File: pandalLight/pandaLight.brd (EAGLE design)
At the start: 90 x 57.4 mm, 113 parts, among them J1 PJ-037A, U1 MIC2230-XXYML, U10 LEDS_CON, U11 LEDS_CON, U12 TPD12S016PWR, U13 M25P40-VMN, U14 PMOD-2X6, U15 PMOD-2X6, U16 PLR135-T10, U17 PLT133-T10W, U18 TP10SQ, U19 TP10SQ, U2 6SLX9TQG144, U20 PAN1322, U3 93LC46BT-I/OT, U4 FT2232HL, U5 TPD12S016PWR, U6 51, U7 51, U8 TXB0104RGYR, U9 100k, X1 USBUB-S, X2 HDMI_RECEPTICAL_A, X3 HDMI_RECEPTICAL_A, Y1 403, Y2 20Mhz

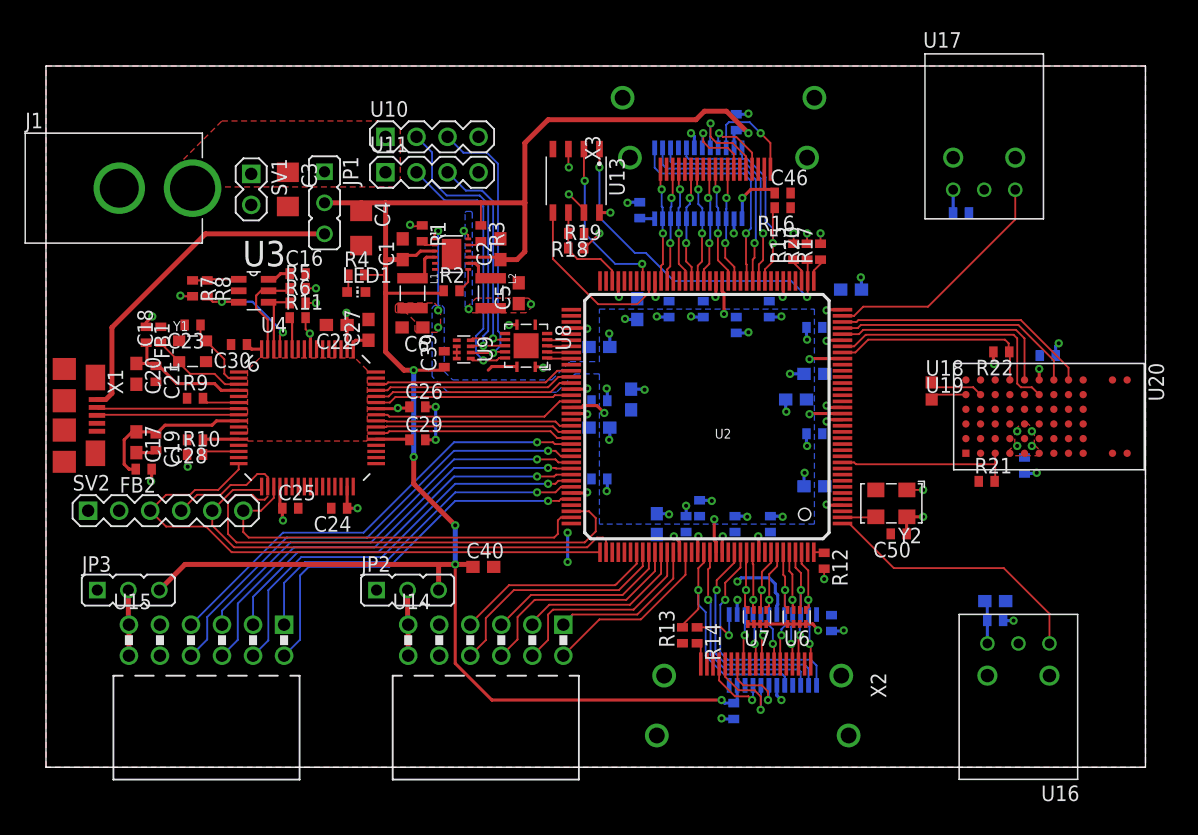
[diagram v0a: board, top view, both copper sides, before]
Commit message: No more airwires! Added ESD protection at 5V_SUP
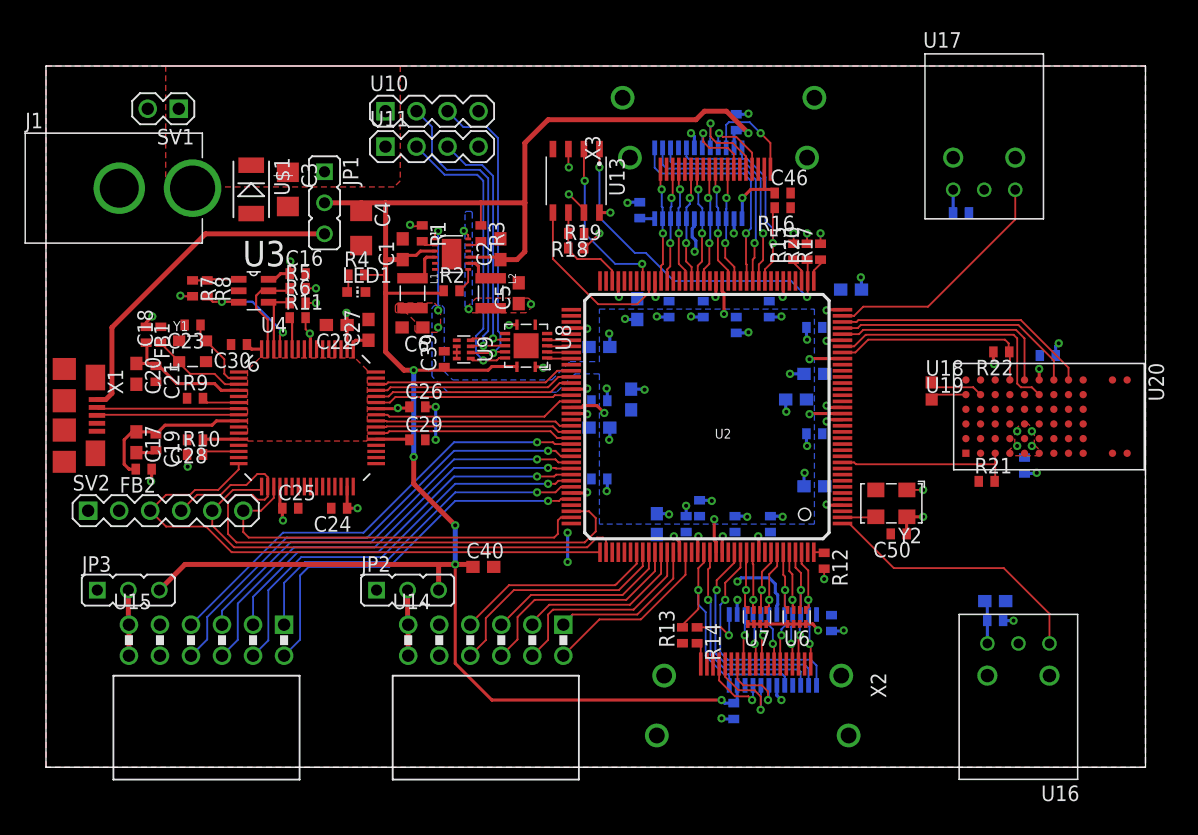
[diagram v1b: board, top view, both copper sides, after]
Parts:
- added U$1: 6V, pandaLight:DO-214AC
- moved SV1 9.77 mm to (9.60, 53.9), turned to 180 degrees
- moved U10 2.10 mm to (31.6, 53.7)
- moved U11 2.10 mm to (31.6, 50.8)
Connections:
- net 5V_SUP: now also U$1.C
- net GND: now also U$1.A
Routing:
- net +5V: track 166.4 -> 170.3 mm
- net LEDS1_DATA_5V: track 24.1 -> 26.2 mm
- net LEDS1_CLK_5V: track 23.7 -> 25.8 mm
- net LEDS0_CLK_5V: track 18.8 -> 20.9 mm
- net LEDS0_DATA_5V: track 22.7 -> 24.8 mm
- net GND: track 51.2 -> 53.3 mm, vias 37 -> 38
- net +3V3: track 70.7 -> 71.9 mm, vias 51 -> 52
- net HDMI_RX_CTRL_EN: track 20.4 -> 21.3 mm
- net USB_TDO: track 49.7 -> 50.5 mm

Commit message: Move S6LX9 to own library; Adjusted parts' "place" layer; USB_PWRSAV#
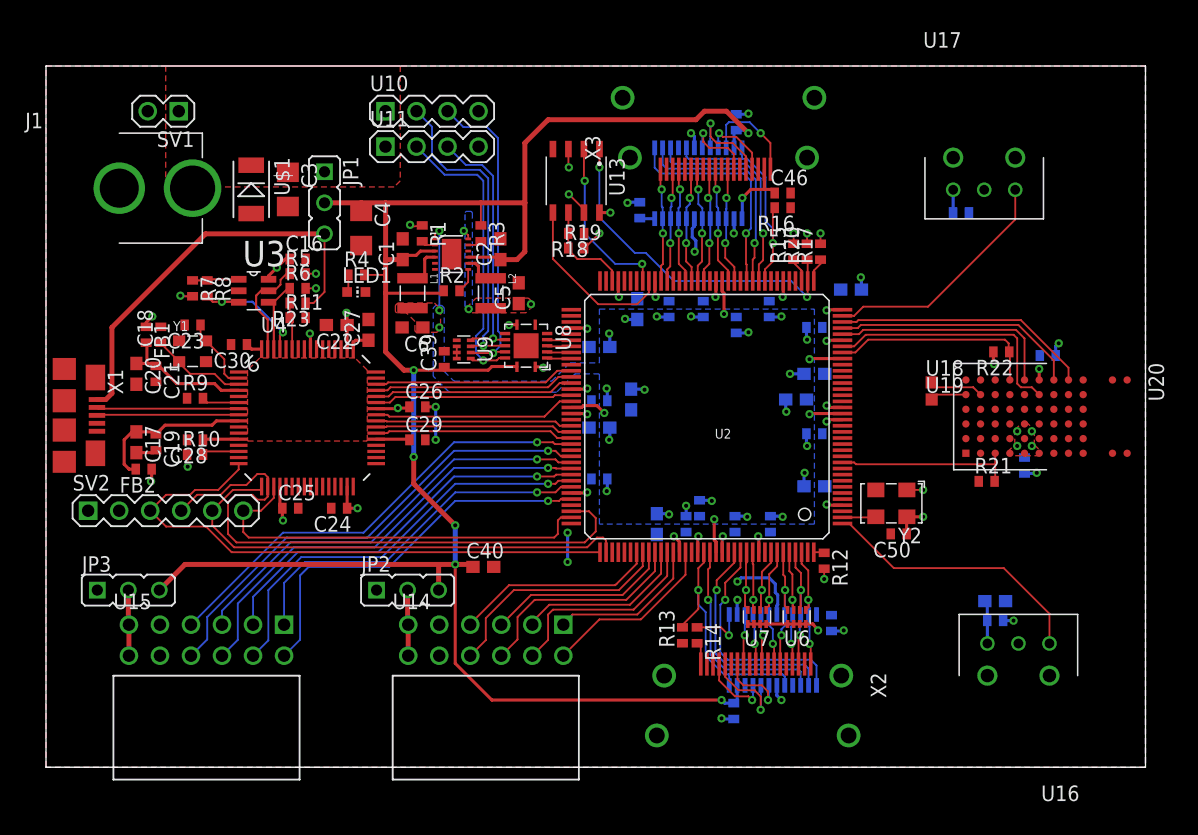
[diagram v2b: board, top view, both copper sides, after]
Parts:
- added R23: 4.7k, pandaLight:0402
- U2: device xilinx_devices_V6:TQ144 -> pandaLight:TQ144
- moved C16 1.20 mm to (20.6, 41.6)
- moved R6 1.20 mm to (20.6, 39.2)
- moved R5 1.20 mm to (20.6, 40.4)
- moved SV1 0.20 mm to (9.60, 53.7)
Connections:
- removed net USB_SUSPEND#: U4.36
- net +3V3: no longer R11.2
- net GND: now also R11.2
- net USB_PWRSAVE#: now also R23.2
- net USB_VBUS: now also R23.1
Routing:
- net USB_VBUS: track 27.4 -> 34.1 mm
- net +3V3: track 71.9 -> 70.1 mm
- net USB_PWRSAVE#: track 2.66 -> 3.86 mm
- net N$6: track 7.77 -> 8.50 mm

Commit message: Part renumber; "place" layer changes
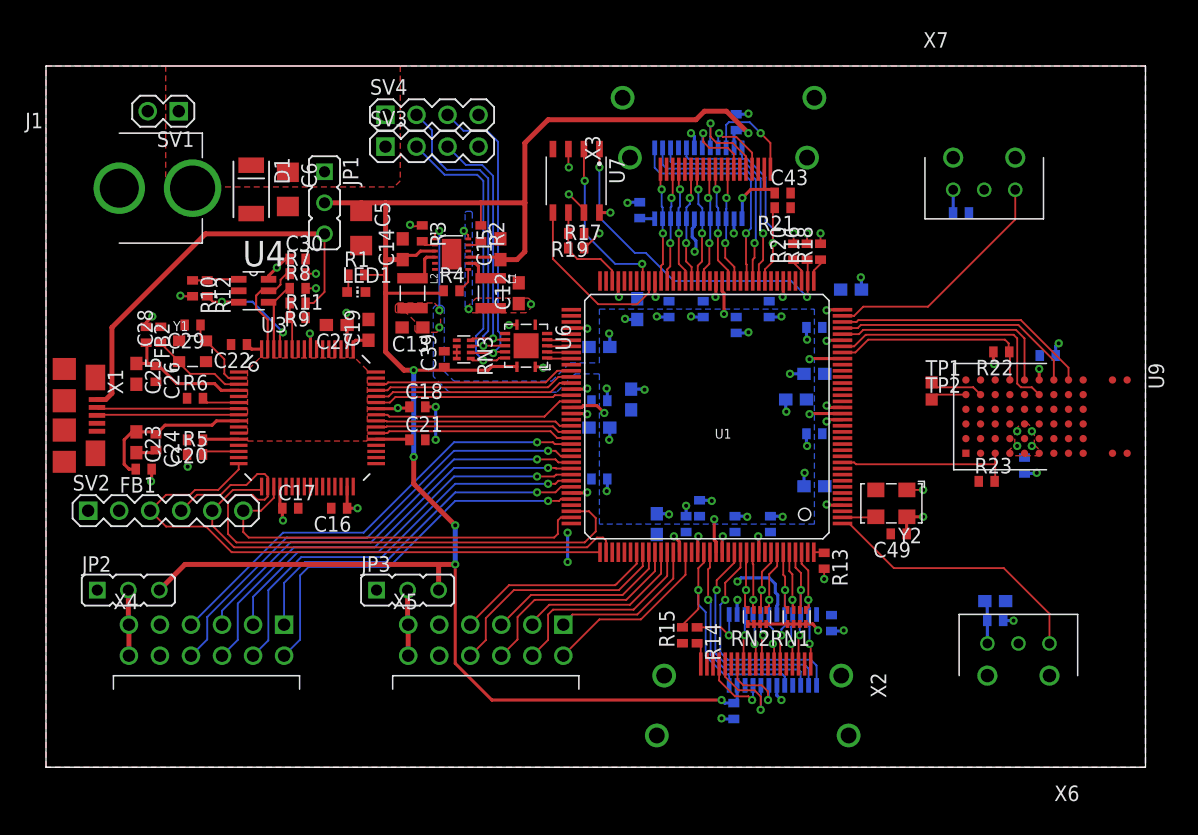
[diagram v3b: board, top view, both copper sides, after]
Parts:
- removed C54: 0.1u, pandaLight:0402
- removed U10: LEDS_CON, pandaLight:MA04-1
- removed U12: TPD12S016PWR, pandaLight:PW_R-PDSO-G24
- removed U13: M25P40-VMN, pandaLight:SO8N
- removed U20: PAN1322, pandaLight:PAN1322
- added RN1, RN2: 51, pandaLight:741C083
- added RN3: 100k, pandaLight:741C083
- added SV4: LEDS_CON, pandaLight:MA04-1
- C10, C11, C41, C47: value 4.7u -> 0.47u; device pandaLight:0603 -> pandaLight:0402
- C12, C13: value 0.47u -> 10u; device pandaLight:0402 -> pandaLight:0603
- C14, C15: value 0.47u -> 4.7u; device pandaLight:0402 -> pandaLight:0603
- C17, C20, C22: value 4.7u -> 0.1u; device pandaLight:0603 -> pandaLight:0402
- C18: value 27p -> 0.1u
- C19, C25, C46: value 0.1u -> 4.7u; device pandaLight:0402 -> pandaLight:0603
- C23: value 27p -> 4.7u; device pandaLight:0402 -> pandaLight:0603
- C28, C29: value 0.1u -> 27p
- C3, C4: value 100u -> 0.47u; device pandaLight:1206 -> pandaLight:0402
- C43, C49: value 0.47u -> 0.1u
- C5, C6: value 10u -> 100u; device pandaLight:0603 -> pandaLight:1206
- JP2: value PMOD2-3_VCC_SEL -> PMOD0-1_VCC_SEL
- JP3: value PMOD0-1_VCC_SEL -> PMOD2-3_VCC_SEL
- R1: value 100k -> 1k
- R12: value 1k -> 2.2k
- R13: value 10k -> 1k
- R15, R21: value 4.7k -> 10k
- R16: value 10k -> 2.4k
- R17: value 4.7k -> 100
- R18: value 100 -> 4.7k
- R20: value 2.4k -> 4.7k
- R4: value 1k -> 100k
- R6: value 10k -> 12k
- R8: value 2.2k -> 10k
- R9: value 12k -> 4.7k
- U1: value MIC2230-XXYML -> 6SLX9TQG144; device pandaLight:MLF-12 -> pandaLight:TQ144
- U2: value 6SLX9TQG144 -> MIC2230-XXYML; device pandaLight:TQ144 -> pandaLight:MLF-12
- U3: value 93LC46BT-I/OT -> FT2232HL; device pandaLight:SOT23-6 -> pandaLight:LQFP64
- U4: value FT2232HL -> 93LC46BT-I/OT; device pandaLight:LQFP64 -> pandaLight:SOT23-6
- U6: value 51 -> TXB0104RGYR; device pandaLight:741C083 -> pandaLight:S-PVQFN-N14
- U7: value 51 -> M25P40-VMN; device pandaLight:741C083 -> pandaLight:SO8N
- U8: value TXB0104RGYR -> TPD12S016PWR; device pandaLight:S-PVQFN-N14 -> pandaLight:PW_R-PDSO-G24
- U9: value 100k -> PAN1322; device pandaLight:741C083 -> pandaLight:PAN1322
- moved R23 58.3 mm to (77.0, 23.4), turned to 0 degrees
- moved R12 55.2 mm to (13.2, 39.2)
- moved U9 48.0 mm to (81.9, 28.7)
- moved U7 38.6 mm to (43.4, 48.0), turned to 270 degrees
- moved C3 38.3 mm to (56.5, 36.2), flipped to the bottom
- moved C4 35.9 mm to (53.5, 21.2), flipped to the bottom, turned to 90 degrees
- moved C51 33.5 mm to (74.9, 45.4), turned to 0 degrees
- moved R15 32.7 mm to (52.1, 10.8)
- moved C14 32.2 mm to (29.2, 42.4), flipped to the top
- moved U6 31.4 mm to (39.3, 34.5), turned to 270 degrees
- moved C15 29.6 mm to (37.2, 42.4), flipped to the top
- moved R21 27.9 mm to (60.3, 45.8), turned to 180 degrees
- moved C2 27.1 mm to (61.4, 30.1), flipped to the bottom, turned to 0 degrees
- moved U1 24.8 mm to (54.1, 28.7), turned to 180 degrees
- moved U2 24.8 mm to (33.2, 42.0), turned to 0 degrees
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- renumbered U$1 to D1, U11 to SV3, U14 to X5, U15 to X4, U16 to X6, U17 to X7, U18 to TP1, U19 to TP2
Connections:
- net +1V2: now also C1.1, C13.1, C2.1, C3.1, C4.1, L2.2, U1.P128, U1.P19, U1.P28, U1.P52, U1.P89, U2.1; no longer C10.1, C12.1, C14.1, C6.1, C8.1, L1.2, U1.1, U2.P128, U2.P19, U2.P28, U2.P52, U2.P89
- net +1V8: now also C19.1, C20.1, C21.1, C22.1, U3.12, U3.37, U3.49, U3.64; no longer C27.1, C28.1, C29.1, C30.1, U4.12, U4.37, U4.49, U4.64
- net +3V3: now also C10.1, C12.1, C17.1, C18.1, C27.1, C30.1, C40.1, C46.1, C51.1, C8.1, L1.2, R10.2, R13.2, R16.2, R18.2, R3.1, R5.1, R8.2, RN1.5, RN1.6, RN1.7, RN1.8, RN2.5, RN2.6, RN2.7, RN2.8, U1.P103, U1.P122, U1.P125, U1.P129, U1.P135, U1.P18, U1.P20, U1.P31, U1.P36, U1.P4, U1.P42, U1.P53, U1.P63, U1.P69, U1.P76, U1.P86, U1.P90, U2.12, U3.20, U3.31, U3.42, U3.50, U3.56, U4.6, U6.1, U7.3, U8.24, U9.A4, U9.A5, U9.A6, U9.B5, U9.C5, U9.F6; no longer C13.1, C15.1, C22.1, C24.1, C25.1, C26.1, C43.1, C5.1, C50.1, C54.1, L2.2, R1.1, R10.1, R12.2, R15.2, R19.2, R5.2, R6.2, U1.12, U12.24, U13.3, U13.7, U13.8, U2.P103, U2.P122, U2.P125, U2.P129, U2.P135, U2.P18, U2.P20, U2.P31, U2.P36, U2.P4, U2.P42, U2.P53, U2.P63, U2.P69, U2.P76, U2.P86, U2.P90, U20.A4, U20.A5, U20.A6, U20.B5, U20.C5, U20.F6, U3.6, U4.20, U4.31, U4.42, U4.50, U4.56, U6.5, U6.6, U6.7, U7.5, U7.6, U8.1, U8.8
- net +5V: now also C14.1, C15.1, C5.1, R1.2, R4.1, U2.3, U2.9, U6.14, U8.11; no longer C1.1, C2.1, C4.1, C40.1, R3.1, R4.2, U1.3, U1.9, U12.11, U8.14
- net 5V_SUP: now also C6.1, SV4.1; no longer C3.1, U10.1
- net BT_CTS: now also U1.P32, U9.F5; no longer U2.P32, U20.F5
- net BT_RESET#: now also R23.2, U1.P11, U9.A3; no longer R21.2, U2.P11, U20.A3
- net BT_RTS: now also U1.P34, U9.F8; no longer U2.P34, U20.F8
- net BT_RX: now also U1.P30, U9.E6; no longer U2.P30, U20.E6
- net BT_TX: now also U1.P33, U9.F7; no longer U2.P33, U20.F7
- net BT_WAKE: now also U1.P29, U9.F4; no longer U2.P29, U20.F4
- net FPGA_CLK20: now also U1.P2; no longer U2.P2
- net GND: now also R15.1, R19.1, R23.1, R6.1, RN3.1, RN3.2, RN3.3, RN3.4, SV4.4, U1.P108, U1.P113, U1.P13, U1.P130, U1.P136, U1.P25, U1.P3, U1.P49, U1.P54, U1.P60, U1.P68, U1.P73, U1.P77, U1.P91, U1.P96, U2.5, U2.6, U2.EP, U3.1, U3.10, U3.11, U3.13, U3.15, U3.25, U3.35, U3.47, U3.5, U3.51, U4.2, U6.7, U6.EP, U7.4, U8.14, U8.19, U8.6, U9.A1, U9.A11, U9.A12, U9.A7, U9.A9, U9.C8, U9.C9, U9.D7, U9.D8, U9.E8, U9.E9, U9.F1, U9.F11, U9.F12, U9.F9; no longer C54.2, R13.1, R16.1, R18.1, R9.1, U1.5, U1.6, U1.EP, U10.4, U12.14, U12.19, U12.6, U13.4, U2.P108, U2.P113, U2.P13, U2.P130, U2.P136, U2.P25, U2.P3, U2.P49, U2.P54, U2.P60, U2.P68, U2.P73, U2.P77, U2.P91, U2.P96, U20.A1, U20.A11, U20.A12, U20.A7, U20.A9, U20.C8, U20.C9, U20.D7, U20.D8, U20.E8, U20.E9, U20.F1, U20.F11, U20.F12, U20.F9, U3.2, U4.1, U4.10, U4.11, U4.13, U4.15, U4.25, U4.35, U4.47, U4.5, U4.51, U8.7, U8.EP, U9.1, U9.2, U9.3, U9.4
- net HDMI_RX_CEC_3V3: now also U1.P132; no longer U2.P132
- net HDMI_RX_CLK_N: now also RN2.4, U1.P133; no longer U2.P133, U7.4
- net HDMI_RX_CLK_P: now also RN2.3, U1.P134; no longer U2.P134, U7.3
- net HDMI_RX_CTRL_EN: now also R15.2, U1.P126; no longer R13.2, U2.P126
- net HDMI_RX_DATA0_N: now also RN2.2, U1.P137; no longer U2.P137, U7.2
- net HDMI_RX_DATA0_P: now also RN2.1, U1.P138; no longer U2.P138, U7.1
- net HDMI_RX_DATA1_N: now also RN1.4, U1.P139; no longer U2.P139, U6.4
- net HDMI_RX_DATA1_P: now also RN1.3, U1.P140; no longer U2.P140, U6.3
- net HDMI_RX_DATA2_N: now also RN1.2, U1.P141; no longer U2.P141, U6.2
- net HDMI_RX_DATA2_P: now also RN1.1, U1.P142; no longer U2.P142, U6.1
- net HDMI_RX_SCL_3V3: now also U1.P131; no longer U2.P131
- net HDMI_RX_SDA_3V3: now also U1.P127; no longer U2.P127
- net HDMI_TX_5V: now also C43.1, U8.13; no longer C46.1, U12.13
- net HDMI_TX_CEC: now also U8.7; no longer U12.7
- net HDMI_TX_CEC_3V3: now also U1.P48, U8.1; no longer U12.1, U2.P48
- net HDMI_TX_CLK_N: now also U1.P50, U8.15; no longer U12.15, U2.P50
- net HDMI_TX_CLK_P: now also U1.P51, U8.16; no longer U12.16, U2.P51
- net HDMI_TX_CTRL_EN: now also R21.2, U1.P45, U8.12, U8.5; no longer R16.2, U12.12, U12.5, U2.P45
- net HDMI_TX_DATA0_N: now also U1.P55, U8.17; no longer U12.17, U2.P55
- net HDMI_TX_DATA0_P: now also U1.P56, U8.18; no longer U12.18, U2.P56
- net HDMI_TX_DATA1_N: now also U1.P57, U8.20; no longer U12.20, U2.P57
- net HDMI_TX_DATA1_P: now also U1.P58, U8.21; no longer U12.21, U2.P58
- net HDMI_TX_DATA2_N: now also U1.P61, U8.22; no longer U12.22, U2.P61
- net HDMI_TX_DATA2_P: now also U1.P62, U8.23; no longer U12.23, U2.P62
- net HDMI_TX_HPD_5V: now also U8.10; no longer U12.10
- net HDMI_TX_SCL_3V3: now also U1.P47, U8.2; no longer U12.2, U2.P47
- net HDMI_TX_SCL_5V: now also U8.8; no longer U12.8
- net HDMI_TX_SDA_3V3: now also U1.P46, U8.3; no longer U12.3, U2.P46
- net HDMI_TX_SDA_5V: now also U8.9; no longer U12.9
- net LEDS0_CLK: now also U1.P78, U6.5; no longer U2.P78, U8.5
- net LEDS0_CLK_5V: now also RN3.8, U6.10; no longer U8.10, U9.8
- net LEDS0_DATA: now also U1.P81, U6.2; no longer U2.P81, U8.2
- net LEDS0_DATA_5V: now also RN3.5, U6.13; no longer U8.13, U9.5
- net LEDS1_CLK: now also U1.P80, U6.3; no longer U2.P80, U8.3
- net LEDS1_CLK_5V: now also RN3.6, SV4.3, U6.12; no longer U10.3, U8.12, U9.6
- net LEDS1_DATA: now also U1.P79, U6.4; no longer U2.P79, U8.4
- net LEDS1_DATA_5V: now also RN3.7, SV4.2, U6.11; no longer U10.2, U8.11, U9.7
- net N$1: now also C29.1, U3.2; no longer C23.1, U4.2
- net N$10: now also R12.2, U3.61, U4.3; no longer R8.2, U3.3, U4.61
- net N$11: now also R6.2, U3.6; no longer R9.2, U4.6
- net N$12: now also R10.1, R12.1, U4.1; no longer R7.1, R8.1, U3.1
- net N$13: now also R5.2, U3.14; no longer R10.2, U4.14
- net N$19: now also U9.E1; no longer U20.E1
- net N$25: now also R2.2, U2.11; no longer R3.2, U1.11
- net N$27: now also R3.2, U2.2; no longer R1.2, U1.2
- net N$28: now also C25.1, C26.1, FB2.2, U3.4; no longer C20.1, C21.1, FB1.2, U4.4
- net N$29: now also U9.E2; no longer U20.E2
- net N$31: now also C23.1, C24.1, FB1.2, U3.9; no longer C17.1, C19.1, FB2.2, U4.9
- net N$34: now also R18.1, U1.P37; no longer R17.1, U2.P37
- net N$35: now also R13.1, U1.P144; no longer R12.1, U2.P144
- net N$36: now also C50.1; no longer C51.1
- net N$39: now also R20.1, U1.P39; no longer R15.1, U2.P39
- net N$4: now also R4.2, U2.7; no longer R2.2, U1.7
- net N$40: now also U1.P64, U7.5; no longer U13.5, U2.P64
- net N$41: now also R16.1, U1.P38, U7.1; no longer R20.1, U13.1, U2.P38
- net N$42: now also R17.1, R19.2, U1.P70, U7.6; no longer R18.2, R19.1, U13.6, U2.P70
- net N$43: now also U1.P65, U7.2; no longer U13.2, U2.P65
- net N$47: now also R1.1; no longer R4.1
- net N$49: now also JP3.2; no longer JP2.2
- net N$5: now also C28.1, U3.3; no longer C18.1, U4.3
- net N$51: now also JP2.2; no longer JP3.2
- net N$6: now also R7.1, U3.63, U4.5; no longer R5.1, U3.5, U4.63
- net N$7: now also U3.7; no longer U4.7
- net N$8: now also U3.8; no longer U4.8
- net N$9: now also R8.1, U3.62, U4.4; no longer R6.1, U3.4, U4.62
- net PMOD0_0: now also U1.P102; no longer U2.P102
- net PMOD0_1: now also U1.P100; no longer U2.P100
- net PMOD0_2: now also U1.P98; no longer U2.P98
- net PMOD0_3: now also U1.P95; no longer U2.P95
- net PMOD1_0: now also U1.P104; no longer U2.P104
- net PMOD1_1: now also U1.P101; no longer U2.P101
- net PMOD1_2: now also U1.P99; no longer U2.P99
- net PMOD1_3: now also U1.P97; no longer U2.P97
- net PMOD2_0: now also U1.P121; no longer U2.P121
- net PMOD2_1: now also U1.P119; no longer U2.P119
- net PMOD2_2: now also U1.P117; no longer U2.P117
- net PMOD2_3: now also U1.P115; no longer U2.P115
- net PMOD3_0: now also U1.P123; no longer U2.P123
- net PMOD3_1: now also U1.P120; no longer U2.P120
- net PMOD3_2: now also U1.P118; no longer U2.P118
- net PMOD3_3: now also U1.P116; no longer U2.P116
- net SW1: now also L1.1, U2.8; no longer L2.1, U1.8
- net SW2: now also L2.1, U2.4; no longer L1.1, U1.4
- net TOS_IN: now also U1.P1; no longer U2.P1
- net TOS_OUT: now also U1.P35; no longer U2.P35
- net USB_CTS#: now also U1.P88, U3.41; no longer U2.P88, U4.41
- net USB_DCD#: now also U1.P84, U3.45; no longer U2.P84, U4.45
- net USB_DSR#: now also U1.P85, U3.44; no longer U2.P85, U4.44
- net USB_DTR#: now also U1.P87, U3.43; no longer U2.P87, U4.43
- net USB_PWRSAVE#: now also R9.2, U3.59; no longer R23.2, U4.59
- net USB_RI#: now also U1.P83, U3.46; no longer U2.P83, U4.46
- net USB_RTS#: now also U1.P92, U3.40; no longer U2.P92, U4.40
- net USB_RXD: now also U1.P93, U3.39; no longer U2.P93, U4.39
- net USB_TCK: now also U1.P109, U3.16; no longer U2.P109, U4.16
- net USB_TDI: now also U1.P110, U3.17; no longer U2.P110, U4.17
- net USB_TDO: now also U1.P106, U3.18; no longer U2.P106, U4.18
- net USB_TMS: now also U1.P107, U3.19; no longer U2.P107, U4.19
- net USB_TXD: now also U1.P94, U3.38; no longer U2.P94, U4.38
- net USB_VBUS: now also R9.1; no longer R23.1
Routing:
- net +5V: track 170.3 -> 168.8 mm

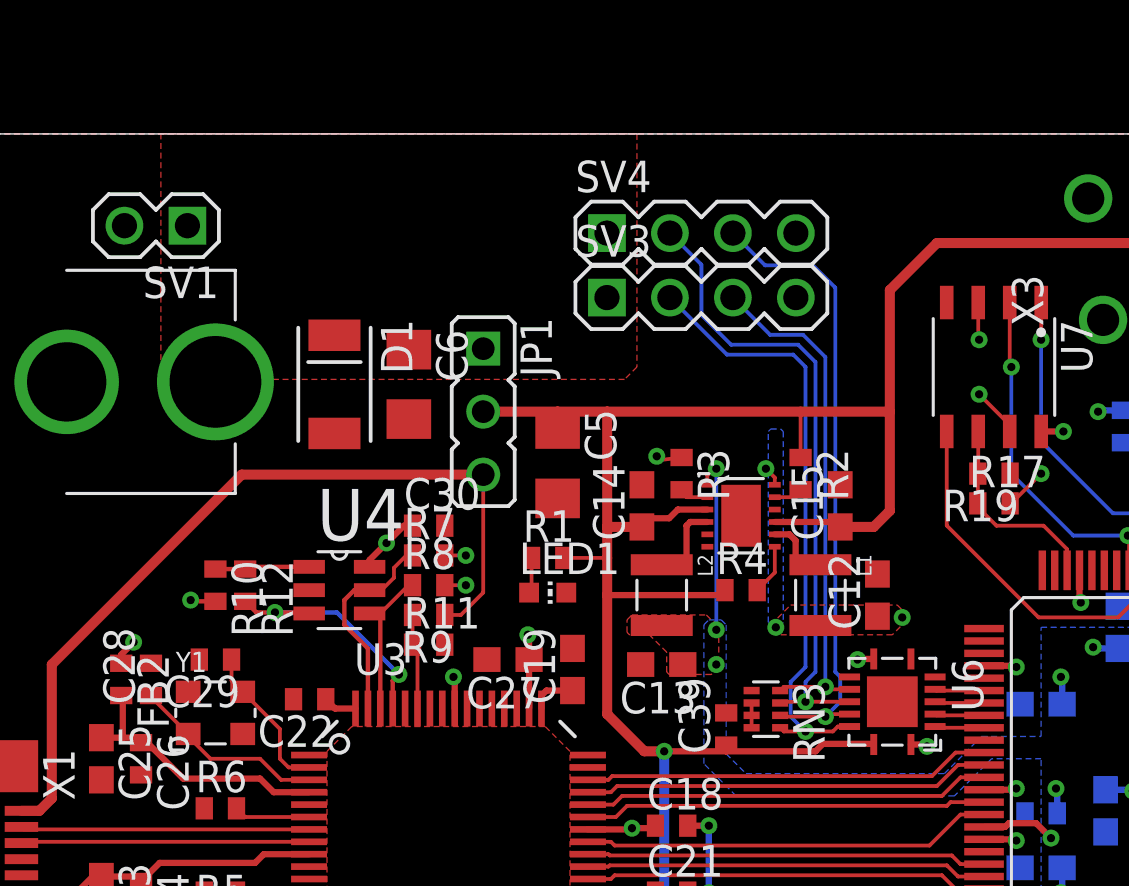
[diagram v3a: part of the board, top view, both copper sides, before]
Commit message: Changed all 7mil traces to 6mil; Set library part prefixes; Applied all part attributes
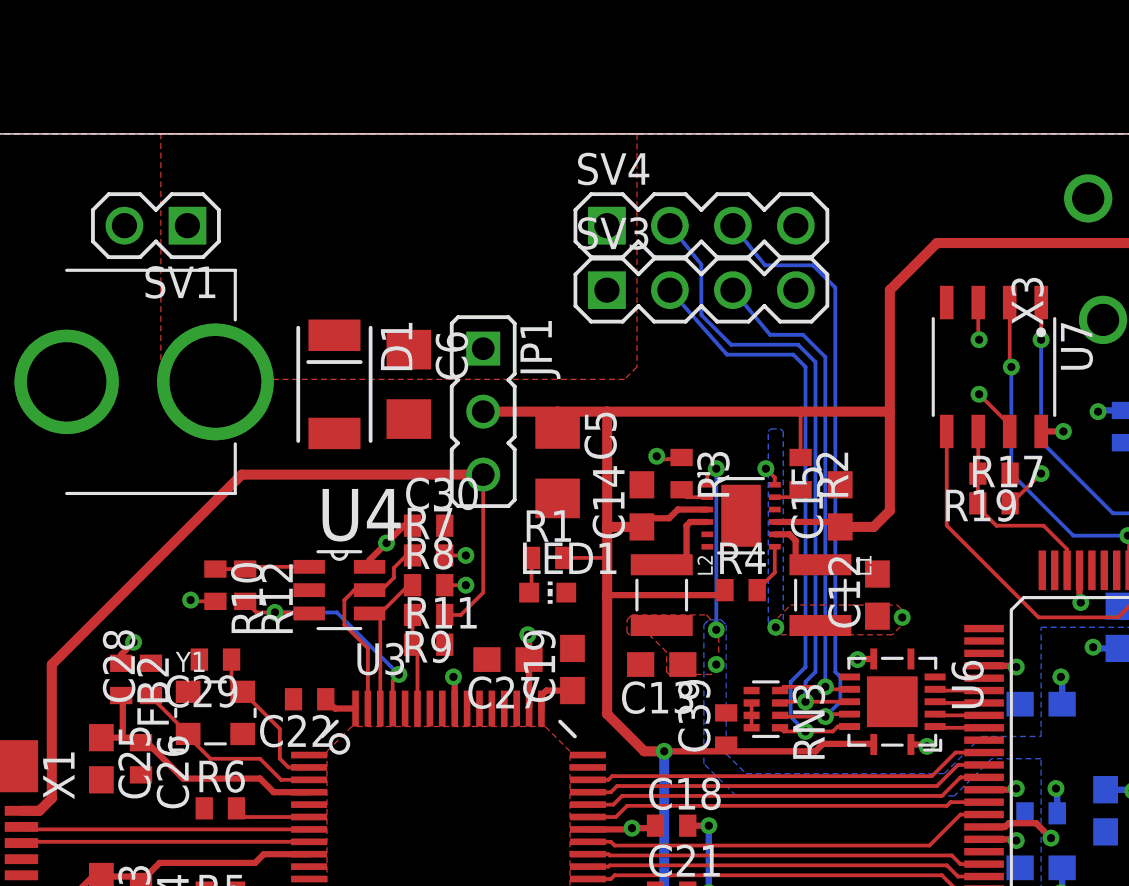
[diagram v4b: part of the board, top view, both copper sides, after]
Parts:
- moved SV3 0.30 mm to (31.6, 51.1)
- moved SV4 0.30 mm to (31.6, 53.7)
